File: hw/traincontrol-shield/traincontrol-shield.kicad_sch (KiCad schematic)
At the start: 3 parts, among them J4 Track Input, J5 Motor Windings, J6 Motor+AC

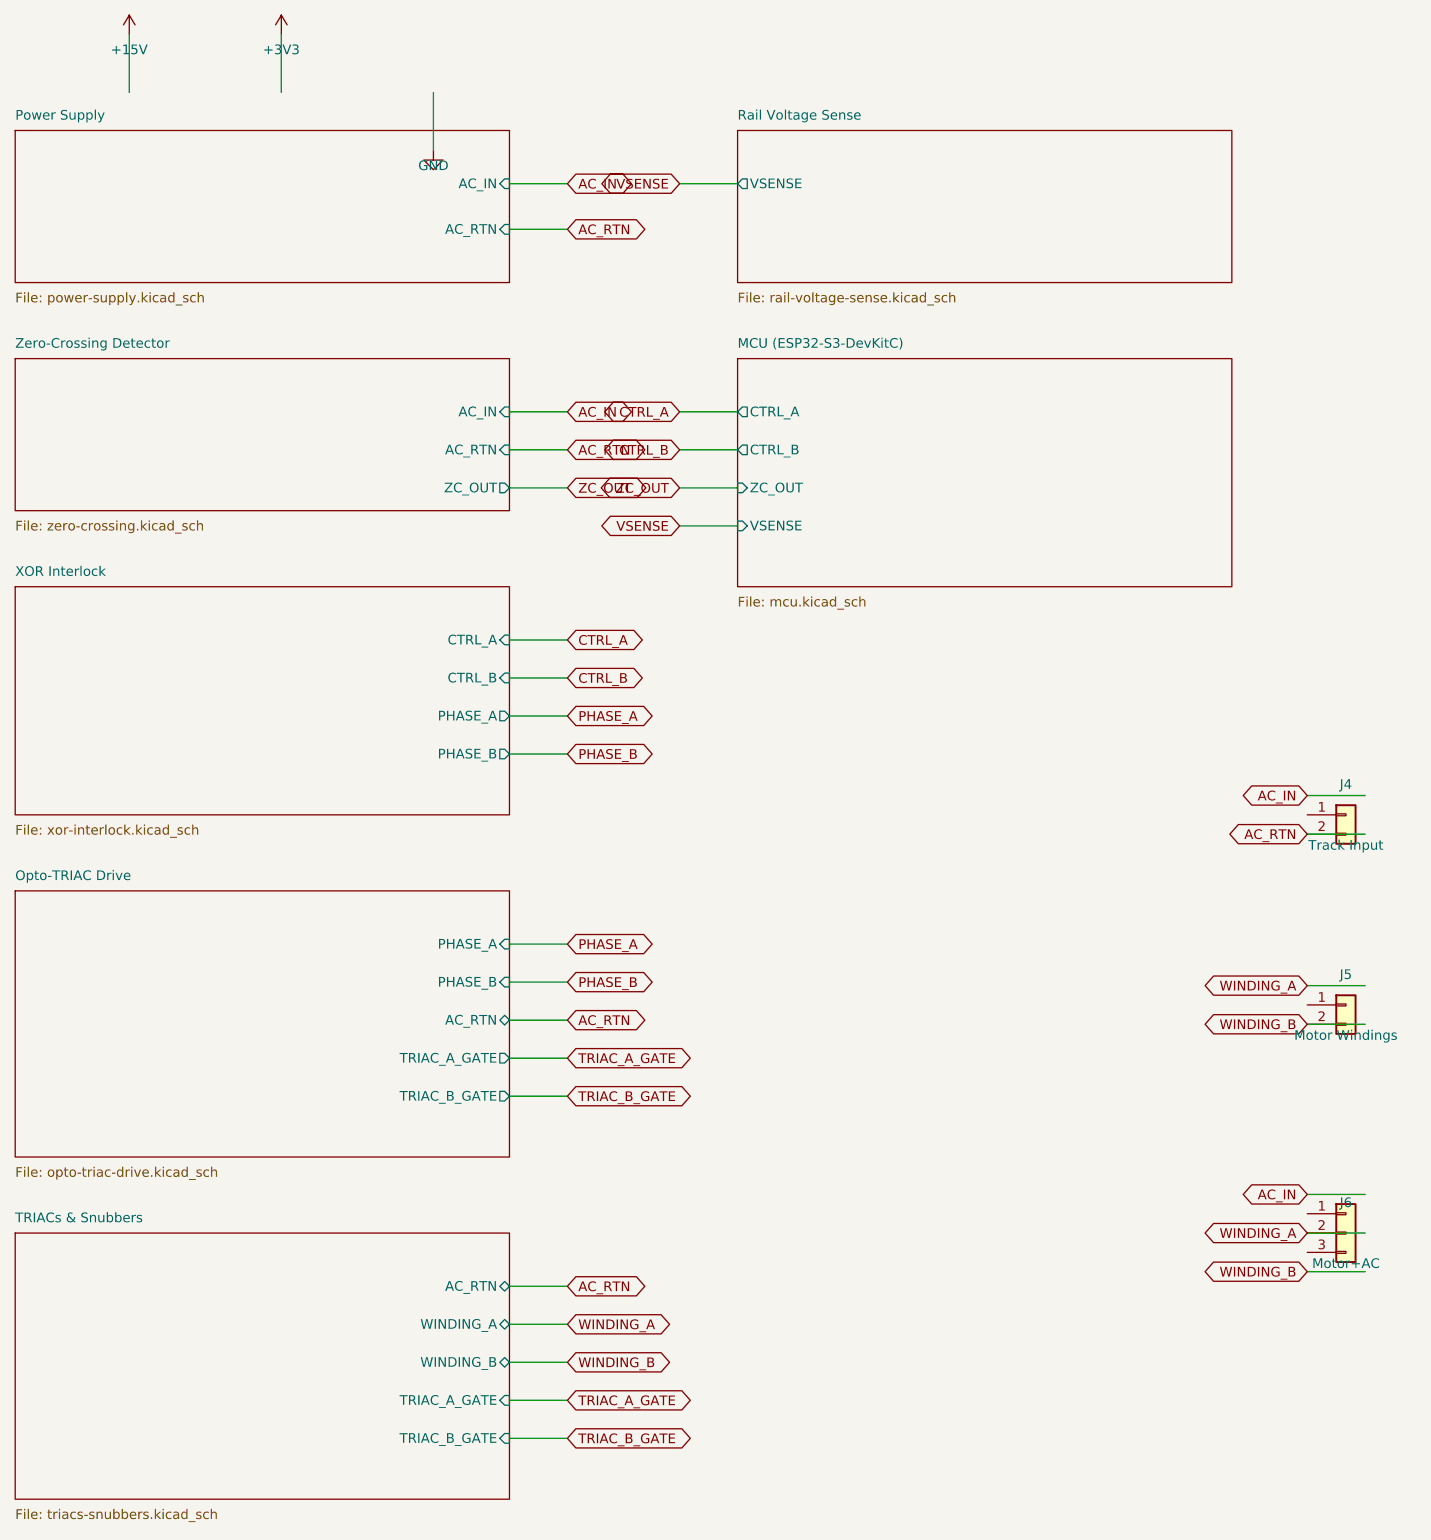
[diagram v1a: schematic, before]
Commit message: Fix schematic ERC errors: pin Y-flip, PWR_FLAG, label wiring, spacing
- Fix connector pin positions using Y-flip convention (sym Y-up → sch Y-down)
- Add GND PWR_FLAG to power-supply sheet (eliminates power_pin_not_driven)
- Fix top-level connector label placement: labels at stub end, wires toward pins
- Apply omnidirectional spacing and IC-to-passive body gap rules across sheets
- Update schematics-plan.md with ERC workflow and coordinate conventions
- Regenerate all sub-sheets with corrected generator scripts

ERC result: 138 violations (all warnings/cosmetic), 0 critical errors.

Co-Authored-By: Claude Opus 4.6 <noreply@anthropic.com>
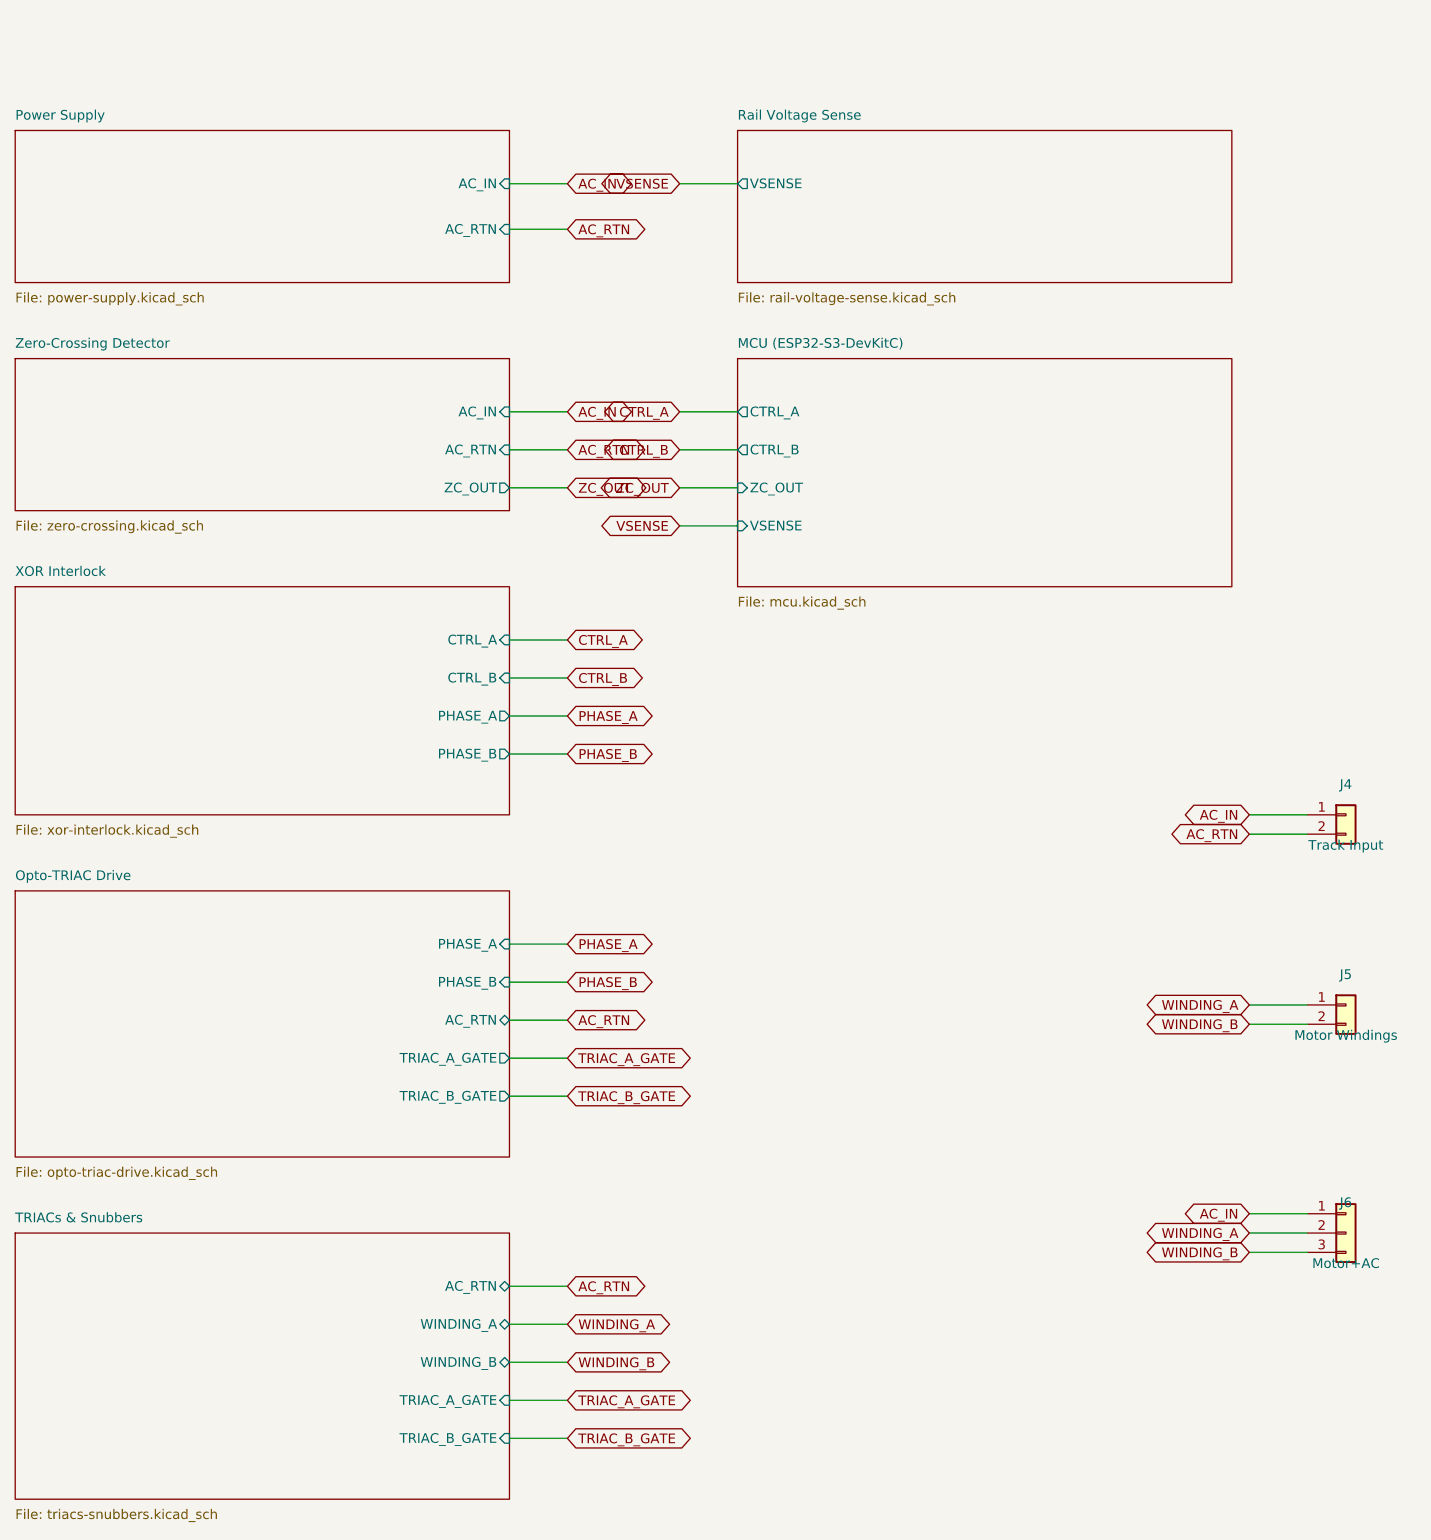
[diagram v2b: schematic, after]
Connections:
- net AC_IN: now also J4.1 (Pin_1), J6.1 (Pin_1)
- net WINDING_A: now also J5.1 (Pin_1)
- net WINDING_B: now also J6.3 (Pin_3)
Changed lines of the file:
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@@
 	)
 	(wire
-		(pts (xy 184.92 107.46) (xy 192.54 107.46))
+		(pts (xy 177.29999999999998 110) (xy 184.92 110))
 		(stroke (width 0) (type solid))
 	)
 	(global_label "AC_IN"
 		(shape bidirectional)
-		(at 184.92 107.46 180)
+		(at 177.29999999999998 110 180)
 		(fields_autoplaced yes)
 		(effects (font (size 1.27 1.27)) (justify right bottom))
 		(property "Intersheetrefs" "${INTERSHEET_REFS}"
-			(at 184.92 107.46 0)
+			(at 177.29999999999998 110 0)
 			(effects (font (size 1.27 1.27)) (hide yes))
 		)
 	)
 	(wire
-		(pts (xy 184.92 112.54) (xy 192.54 112.54))
+		(pts (xy 177.29999999999998 112.54) (xy 184.92 112.54))
 		(stroke (width 0) (type solid))
 	)
 	(global_label "AC_RTN"
 		(shape bidirectional)
-		(at 184.92 112.54 180)
+		(at 177.29999999999998 112.54 180)
 		(fields_autoplaced yes)
 		(effects (font (size 1.27 1.27)) (justify right bottom))
 		(property "Intersheetrefs" "${INTERSHEET_REFS}"
-			(at 184.92 112.54 0)
+			(at 177.29999999999998 112.54 0)
 			(effects (font (size 1.27 1.27)) (hide yes))
 		)
@@
 	)
 	(wire
-		(pts (xy 184.92 132.46) (xy 192.54 132.46))
+		(pts (xy 177.29999999999998 135) (xy 184.92 135))
 		(stroke (width 0) (type solid))
 	)
 	(global_label "WINDING_A"
 		(shape bidirectional)
-		(at 184.92 132.46 180)
+		(at 177.29999999999998 135 180)
 		(fields_autoplaced yes)
 		(effects (font (size 1.27 1.27)) (justify right bottom))
 		(property "Intersheetrefs" "${INTERSHEET_REFS}"
-			(at 184.92 132.46 0)
+			(at 177.29999999999998 135 0)
 			(effects (font (size 1.27 1.27)) (hide yes))
 		)
 	)
 	(wire
-		(pts (xy 184.92 137.54) (xy 192.54 137.54))
+		(pts (xy 177.29999999999998 137.54) (xy 184.92 137.54))
 		(stroke (width 0) (type solid))
 	)
 	(global_label "WINDING_B"
 		(shape bidirectional)
-		(at 184.92 137.54 180)
+		(at 177.29999999999998 137.54 180)
 		(fields_autoplaced yes)
 		(effects (font (size 1.27 1.27)) (justify right bottom))
 		(property "Intersheetrefs" "${INTERSHEET_REFS}"
-			(at 184.92 137.54 0)
+			(at 177.29999999999998 137.54 0)
 			(effects (font (size 1.27 1.27)) (hide yes))
 		)
@@
 	)
 	(wire
-		(pts (xy 184.92 159.92) (xy 192.54 159.92))
+		(pts (xy 177.29999999999998 162.46) (xy 184.92 162.46))
 		(stroke (width 0) (type solid))
 	)
 	(global_label "AC_IN"
 		(shape bidirectional)
-		(at 184.92 159.92 180)
+		(at 177.29999999999998 162.46 180)
 		(fields_autoplaced yes)
 		(effects (font (size 1.27 1.27)) (justify right bottom))
 		(property "Intersheetrefs" "${INTERSHEET_REFS}"
-			(at 184.92 159.92 0)
+			(at 177.29999999999998 162.46 0)
 			(effects (font (size 1.27 1.27)) (hide yes))
 		)
 	)
 	(wire
-		(pts (xy 184.92 165.0) (xy 192.54 165.0))
+		(pts (xy 177.29999999999998 165) (xy 184.92 165))
 		(stroke (width 0) (type solid))
 	)
 	(global_label "WINDING_A"
 		(shape bidirectional)
-		(at 184.92 165.0 180)
+		(at 177.29999999999998 165 180)
 		(fields_autoplaced yes)
 		(effects (font (size 1.27 1.27)) (justify right bottom))
 		(property "Intersheetrefs" "${INTERSHEET_REFS}"
-			(at 184.92 165.0 0)
+			(at 177.29999999999998 165 0)
 			(effects (font (size 1.27 1.27)) (hide yes))
 		)
 	)
 	(wire
-		(pts (xy 184.92 170.08) (xy 192.54 170.08))
+		(pts (xy 177.29999999999998 167.54) (xy 184.92 167.54))
 		(stroke (width 0) (type solid))
 	)
 	(global_label "WINDING_B"
 		(shape bidirectional)
-		(at 184.92 170.08 180)
+		(at 177.29999999999998 167.54 180)
 		(fields_autoplaced yes)
 		(effects (font (size 1.27 1.27)) (justify right bottom))
 		(property "Intersheetrefs" "${INTERSHEET_REFS}"
-			(at 184.92 170.08 0)
+			(at 177.29999999999998 167.54 0)
 			(effects (font (size 1.27 1.27)) (hide yes))
 		)
 	)
-	(wire
-		(pts (xy 30 15) (xy 30 7.38))
-		(stroke (width 0) (type solid))
-	)
-	(symbol
-		(lib_id "power:+15V")
-		(at 30 7.38 0)
-		(unit 1)
-		(exclude_from_sim no)
-		(in_bom no)
-		(on_board yes)
-		(dnp no)
-		(property "Reference" "#PWR0101"
-			(at 30 5.38 0)
-			(effects (font (size 1.27 1.27)) (hide yes))
-		)
-		(property "Value" "+15V"
-			(at 30 9.379999999999999 0)
-			(effects (font (size 1.27 1.27)))
-		)
-		(property "Footprint" ""
-			(at 30 7.38 0)
-			(effects (font (size 1.27 1.27)) (hide yes))
-		)
-		(property "Datasheet" ""
-			(at 30 7.38 0)
-			(effects (font (size 1.27 1.27)) (hide yes))
-		)
-		(pin "1")
-		(instances
-			(project "traincontrol-shield"
-				(path "/12cc2a67-9b1c-41e4-828f-9c2a8df6bb35"
-					(reference "#PWR0101")
-					(unit 1)
-				)
-			)
-		)
-	)
-	(wire
-		(pts (xy 50 15) (xy 50 7.38))
-		(stroke (width 0) (type solid))
-	)
-	(symbol
-		(lib_id "power:+3V3")
-		(at 50 7.38 0)
-		(unit 1)
-		(exclude_from_sim no)
-		(in_bom no)
-		(on_board yes)
-		(dnp no)
-		(property "Reference" "#PWR0102"
-			(at 50 5.38 0)
-			(effects (font (size 1.27 1.27)) (hide yes))
-		)
-		(property "Value" "+3V3"
-			(at 50 9.379999999999999 0)
-			(effects (font (size 1.27 1.27)))
-		)
-		(property "Footprint" ""
-			(at 50 7.38 0)
-			(effects (font (size 1.27 1.27)) (hide yes))
-		)
-		(property "Datasheet" ""
-			(at 50 7.38 0)
-			(effects (font (size 1.27 1.27)) (hide yes))
-		)
-		(pin "1")
-		(instances
-			(project "traincontrol-shield"
-				(path "/12cc2a67-9b1c-41e4-828f-9c2a8df6bb35"
-					(reference "#PWR0102")
-					(unit 1)
-				)
-			)
-		)
-	)
-	(wire
-		(pts (xy 70 15) (xy 70 22.62))
-		(stroke (width 0) (type solid))
-	)
-	(symbol
-		(lib_id "power:GND")
-		(at 70 22.62 0)
-		(unit 1)
-		(exclude_from_sim no)
-		(in_bom no)
-		(on_board yes)
-		(dnp no)
-		(property "Reference" "#PWR0103"
-			(at 70 20.62 0)
-			(effects (font (size 1.27 1.27)) (hide yes))
-		)
-		(property "Value" "GND"
-			(at 70 24.62 0)
-			(effects (font (size 1.27 1.27)))
-		)
-		(property "Footprint" ""
-			(at 70 22.62 0)
-			(effects (font (size 1.27 1.27)) (hide yes))
-		)
-		(property "Datasheet" ""
-			(at 70 22.62 0)
-			(effects (font (size 1.27 1.27)) (hide yes))
-		)
-		(pin "1")
-		(instances
-			(project "traincontrol-shield"
-				(path "/12cc2a67-9b1c-41e4-828f-9c2a8df6bb35"
-					(reference "#PWR0103")
-					(unit 1)
-				)
-			)
-		)
-	)
